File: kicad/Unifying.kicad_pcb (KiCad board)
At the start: 4 copper layers, 120.9 x 78.8 mm, 132 parts, among them J1 Conn_01x02, J10 GPDI0, J11 GPDI1, J12 nRpiBoot, J13 Conn_01x03, J14 Conn_01x03, J15 AudioOUT, J16 Micro_SD_Card_Det, J17 THD-20-R, J18 GLOBAL_EN, J19 AudioAMP, J2 Bus_M.2_Socket_B, J20 THD-02-R, J21 MIC, J3 USB_OTG, J4 Conn_01x04_Male, J5 USB_A, J6 USB_A, J7 USB_MICRO, J8 Conn_01x22_Female, J9 Conn_01x22_Female, Q1 DMP3013SFV-7, U1 TPD4EUSB30, U10 74LVC1G07SE-7, U11 RT9742GGJ5, U12 MagJack-A70-112-331N126, U2 AP64501SP-13, U3 FSUSB42MUX, U4 USB2514B-I/M2, U5 TPD4EUSB30, U6 AP22653W6, U7 RT9742SNGV, U8 74LVC1G07SE-7, U9 NC7WZ16, Y1 24MHz

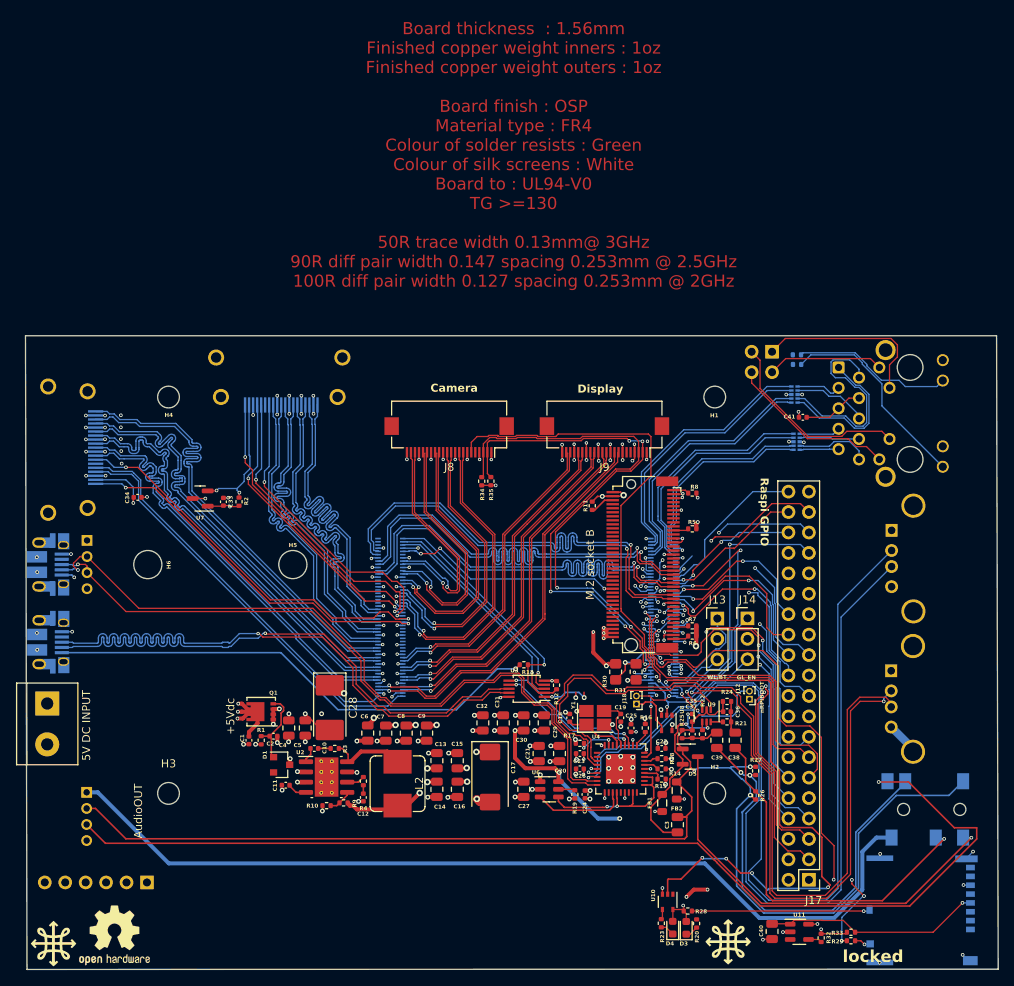
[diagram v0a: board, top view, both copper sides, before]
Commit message: Rounting all signals fix #16
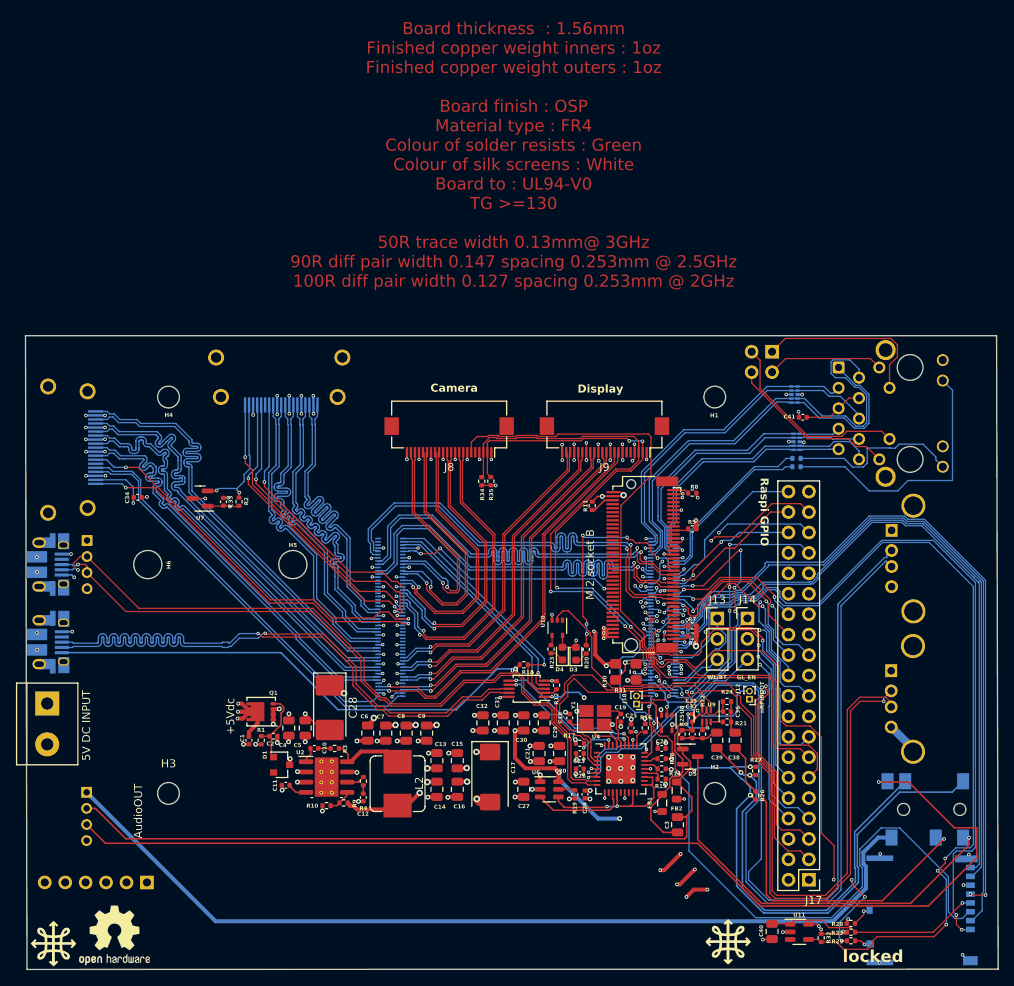
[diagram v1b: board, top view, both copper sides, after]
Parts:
- moved D3 36.7 mm to (165.2, 114.0)
- moved D4 36.7 mm to (163.5, 113.9)
- moved R20 36.7 mm to (166.5, 113.4)
- moved R23 36.7 mm to (162.1, 113.4)
- moved U10 36.7 mm to (162.9, 110.7)
- moved R28 20.3 mm to (199.4, 147.5)
- moved R36 13.9 mm to (192.6, 90.7)
- moved R37 11.7 mm to (192.7, 89.7)
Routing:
- net /CM4_GPIO (GPIO, SDCARD)/SD_PWR_ON: track 1.70 -> 114.2 mm, vias 0 -> 3
- net /CM4_GPIO (GPIO, SDCARD)/SD_DAT2: track 0.00 -> 95.3 mm, vias 0 -> 2
- net /CM4_GPIO (GPIO, SDCARD)/SD_DAT3: track 0.00 -> 91.8 mm
- net /CM4_GPIO (GPIO, SDCARD)/SD_CLK: track 0.00 -> 89.6 mm, vias 0 -> 2
- net /CM4_GPIO (GPIO, SDCARD)/SD_CMD: track 0.00 -> 88.2 mm, vias 0 -> 2
- net /CM4_GPIO (GPIO, SDCARD)/SD_DAT0: track 0.00 -> 85.8 mm
- net /CM4_GPIO (GPIO, SDCARD)/SD_DAT1: track 0.00 -> 85.3 mm
- net /CM4_GPIO (GPIO, SDCARD)/nPWR_LED: track 70.5 -> 22.5 mm, vias 5 -> 1
- net Net-(Module1A-PI_nLED_Activity): track 2.95 -> 28.3 mm, vias 0 -> 5
- net /CM4_GPIO (GPIO, SDCARD)/ETH_LEDY: track 0.00 -> 21.6 mm
- net /CM4_GPIO (GPIO, SDCARD)/ETH_LEDG: track 0.00 -> 21.4 mm
- net Net-(J16-DET_A): track 22.2 -> 2.80 mm
- net Net-(U12-LEDG_K): track 19.9 -> 33.6 mm
- net /USB2-HUB/VBUS: track 184.1 -> 190.5 mm, vias 8 -> 12
- net /CM4_GPIO (GPIO, SDCARD)/GPIO11: track 29.9 -> 26.1 mm
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
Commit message: Slightly improving routing
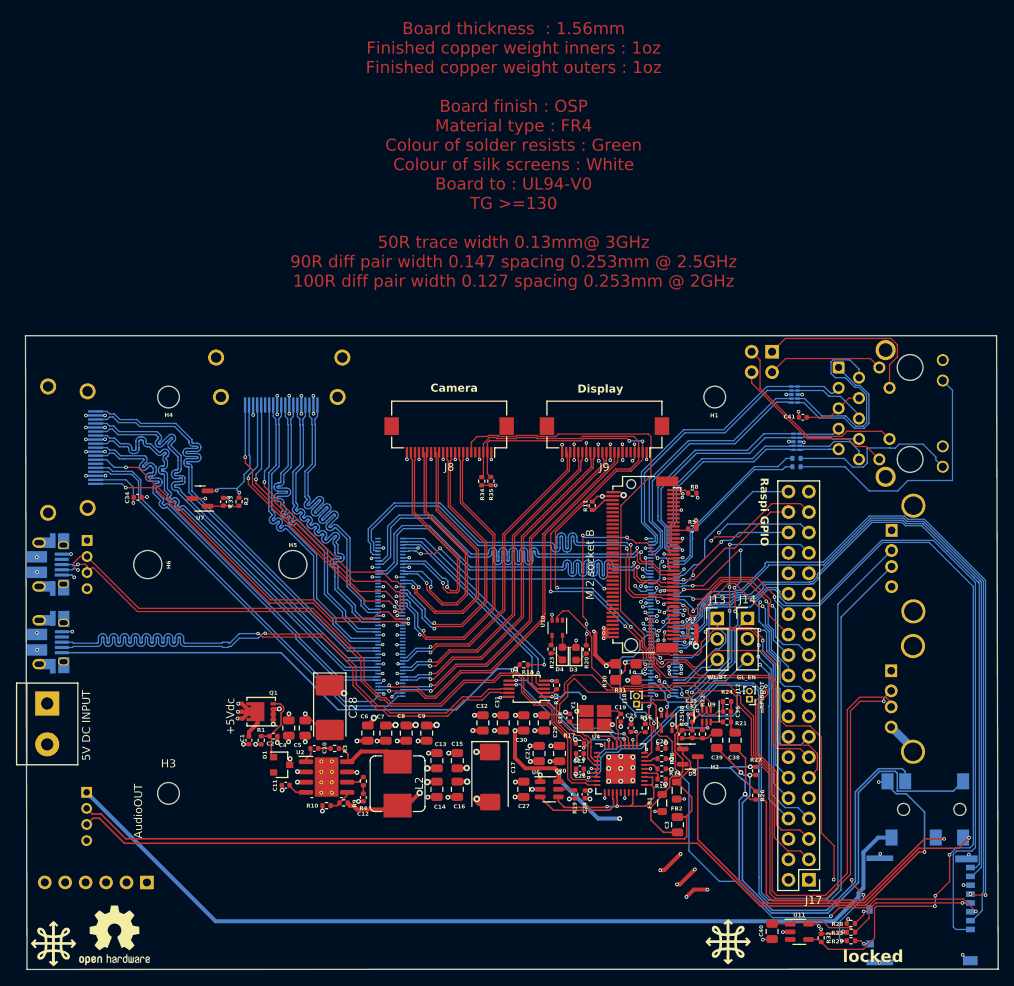
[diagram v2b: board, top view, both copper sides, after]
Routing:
- net Net-(J19-Pin_3): track 136.8 -> 124.4 mm, vias 1 -> 2
- net /CM4_GPIO (GPIO, SDCARD)/SD_CMD: track 88.2 -> 75.9 mm, vias 2 -> 4
- net Net-(D5-K)_1: track 169.2 -> 174.8 mm
- net /CM4_GPIO (GPIO, SDCARD)/AUDIO_R: track 53.1 -> 56.7 mm
- net /USB2-HUB/HD3_P: track 110.5 -> 107.7 mm
- net /USB2-HUB/HD3_N: track 110.6 -> 109.1 mm
- net /CM4_GPIO (GPIO, SDCARD)/SD_PWR_ON: track 114.2 -> 113.0 mm
- net /CM4_GPIO (GPIO, SDCARD)/SD_PWR: track 27.0 -> 27.7 mm
- net Net-(D5-K): track 52.0 -> 51.5 mm
- net /CM4_GPIO (GPIO, SDCARD)/SD_DAT2: track 95.3 -> 95.7 mm, vias 2 -> 0

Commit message: Adding/moving some text fix #19
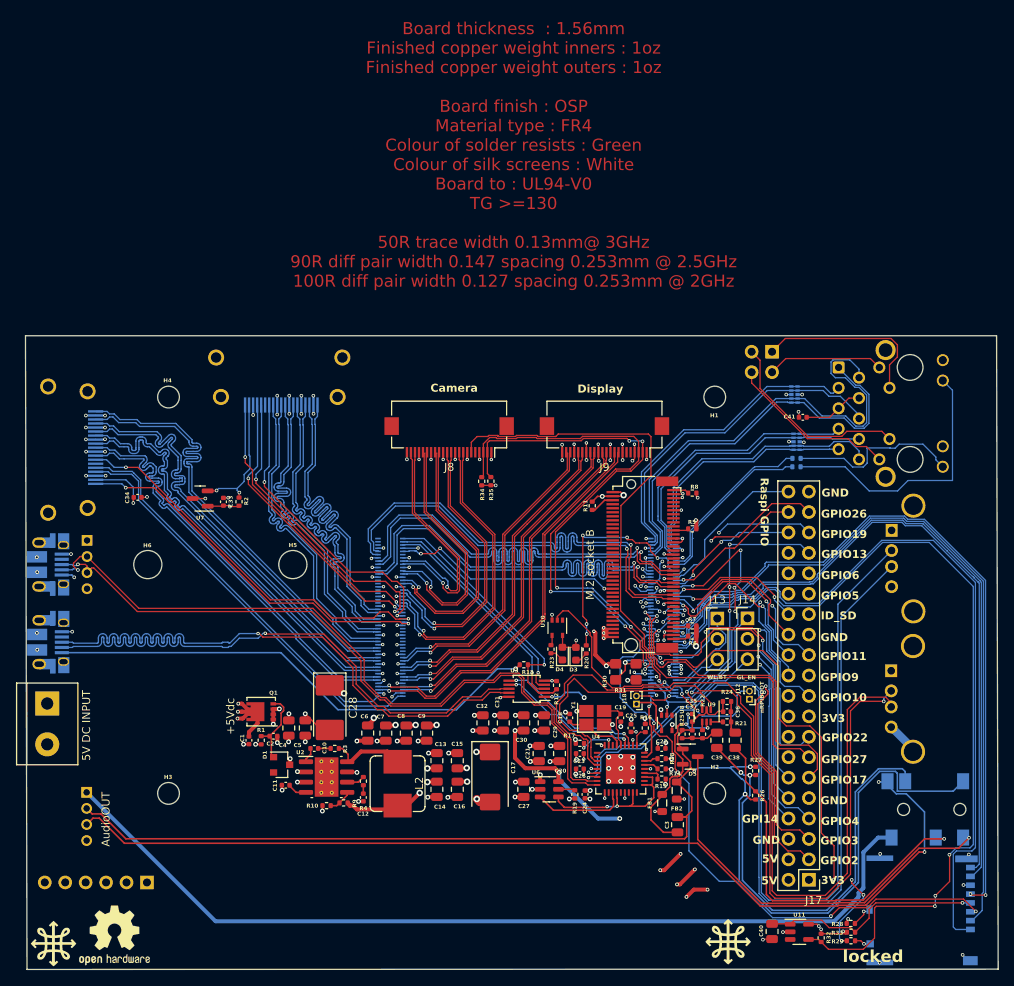
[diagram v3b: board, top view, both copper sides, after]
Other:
- board text added: "3V3"
- board text added: "5V"
- board text added: "GND"
- board text added: "GPI14"
- board text added: "GPIO10"
- board text added: "GPIO11"
- board text added: "GPIO13"
- board text added: "GPIO17"
- board text added: "GPIO19"
- board text added: "GPIO2"
- board text added: "GPIO22"
- board text added: "GPIO26"
- board text added: "GPIO27"
- board text added: "GPIO3"
- board text added: "GPIO4"
- board text added: "GPIO5"
- board text added: "GPIO6"
- board text added: "GPIO9"
- board text added: "ID_SD"
- board text added: "Microphone"
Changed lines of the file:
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@@
     (property "ki_description" "Mounting Hole without connection")
     (property "ki_keywords" "mounting hole")
-    (fp_text reference "H6" (at 2.601 0.04 90) (layer "F.SilkS")
+    (fp_text reference "H6" (at -0.059 -2.38 180) (layer "F.SilkS")
         (effects (font (size 0.5 0.5) (thickness 0.1) bold))
     )
@@
     (property "ki_description" "Mounting Hole without connection")
     (property "ki_keywords" "mounting hole")
-    (fp_text reference "H3" (at 0 -3.7) (layer "F.SilkS")
-        (effects (font (size 1 1) (thickness 0.15)))
+    (fp_text reference "H3" (at -0.052 -2.028) (layer "F.SilkS")
+        (effects (font (size 0.5 0.5) (thickness 0.1) bold))
     )
     (fp_text value "MountingHole" (at 0.068 0.762) (layer "F.Fab")
@@
     (property "ki_keywords" "cap capacitor")
     (attr smd)
-    (fp_text reference "C28" (at 0 -2.89 -90) (layer "F.SilkS")
+    (fp_text reference "C28" (at 0 -2.89 90) (layer "F.SilkS")
         (effects (font (size 1 1) (thickness 0.15)))
     )
-    (fp_text value "100uF" (at 0 2.7 -90) (layer "F.Fab")
+    (fp_text value "100uF" (at 0 2.7 90) (layer "F.Fab")
         (effects (font (size 1 1) (thickness 0.15)))
     )
-    (fp_text user "${REFERENCE}" (at 0 0 -90) (layer "F.Fab")
+    (fp_text user "${REFERENCE}" (at 0 0 90) (layer "F.Fab")
         (effects (font (size 1 1) (thickness 0.15)))
     )
@@
       (rotate (xyz 0 0 0))
     )
+    (model ":KICAD6_3DMODEL_DIR:Capacitor_Tantalum_SMD.3dshapes/CP_EIA-7343-20_Kemet-V.wrl"
+      (offset (xyz 0 0 0))
+      (scale (xyz 0.9 0.9 0.9))
+      (rotate (xyz 0 0 0))
+    )
   )
   (footprint "Capacitor_SMD:C_0402_1005Metric" (layer "F.Cu")
@@
     (property "ki_description" "Mounting Hole without connection")
     (property "ki_keywords" "mounting hole")
-    (fp_text reference "H4" (at 0.028 2.238) (layer "F.SilkS")
+    (fp_text reference "H4" (at -0.122 -2.062) (layer "F.SilkS")
         (effects (font (size 0.5 0.5) (thickness 0.1) bold))
     )
@@
         (effects (font (size 1 1) (thickness 0.15)) (justify mirror))
     )
-    (fp_text user "${VALUE}" (at -0.204 -97.843 90 unlocked) (layer "F.SilkS")
+    (fp_text user "${VALUE}" (at -1.22 -101.88 90 unlocked) (layer "F.SilkS")
         (effects (font (size 1 1) (thickness 0.15)))
     )
@@
     (property "Sheetname" "CM4_GPIO (GPIO, SDCARD)")
     (attr through_hole)
-    (fp_text reference "U12" (at 0.01 11.32 90) (layer "B.SilkS")
+    (fp_text reference "U12" (at -6.84 11.3925 90) (layer "B.SilkS")
         (effects (font (size 1 1) (thickness 0.15)) (justify mirror))
     )
@@
     (property "ki_keywords" "connector")
     (attr through_hole)
-    (fp_text reference "J21" (at 0 2.77 90) (layer "B.SilkS")
+    (fp_text reference "J21" (at -2.6 0.68 180) (layer "B.SilkS")
         (effects (font (size 1 1) (thickness 0.15)) (justify mirror))
     )
@@
     (effects (font (size 1 1) (thickness 0.15)) (justify mirror))
   )
-  (gr_text "GPDI1" (at 135.52 90.08) (layer "B.SilkS")
+  (gr_text "GPDI1" (at 135.46 85.29) (layer "B.SilkS")
     (effects (font (size 1 1) (thickness 0.2) bold) (justify mirror))
   )
-  (gr_text "USB3" (at 196.2 100.43 90) (layer "B.SilkS")
+  (gr_text "USB3" (at 212.5 94.51) (layer "B.SilkS")
     (effects (font (size 1 1) (thickness 0.2) bold) (justify mirror))
   )
+  (gr_text "Microphone" (at 113.62 140.42) (layer "B.SilkS")
+    (effects (font (size 1 1) (thickness 0.2) bold) (justify left bottom mirror))
+  )
   (gr_text "uSDCARD" (at 216.77 147.48 -90) (layer "B.SilkS")
     (effects (font (size 1 1) (thickness 0.2) bold) (justify mirror))
   )
-  (gr_text "GPDI0" (at 110.02 82.73 90) (layer "B.SilkS")
+  (gr_text "GPDI0" (at 107.83 81.66 90) (layer "B.SilkS")
     (effects (font (size 1 1) (thickness 0.2) bold) (justify mirror))
   )
-  (gr_text "USB2" (at 196.2 117.26 90) (layer "B.SilkS")
+  (gr_text "USB2" (at 212.62 112.27) (layer "B.SilkS")
     (effects (font (size 1 1) (thickness 0.2) bold) (justify mirror))
   )
@@
     (effects (font (size 2 2) (thickness 0.3)) (justify mirror))
   )
+  (gr_text "GPIO22" (at 195.81 124.96) (layer "F.SilkS")
+    (effects (font (size 1 1) (thickness 0.2) bold) (justify left bottom))
+  )
+  (gr_text "3V3" (at 195.68 142.69) (layer "F.SilkS")
+    (effects (font (size 1 1) (thickness 0.2) bold) (justify left bottom))
+  )
+  (gr_text "GPIO9" (at 195.63 117.46) (layer "F.SilkS")
+    (effects (font (size 1 1) (thickness 0.2) bold) (justify left bottom))
+  )
+  (gr_text "GPIO11" (at 195.64 114.85) (layer "F.SilkS")
+    (effects (font (size 1 1) (thickness 0.2) bold) (justify left bottom))
+  )
+  (gr_text "GND" (at 195.75 94.53) (layer "F.SilkS")
+    (effects (font (size 1 1) (thickness 0.2) bold) (justify left bottom))
+  )
+  (gr_text "GPIO5" (at 195.68 107.32) (layer "F.SilkS")
+    (effects (font (size 1 1) (thickness 0.2) bold) (justify left bottom))
+  )
+  (gr_text "3V3" (at 195.73 122.56) (layer "F.SilkS")
+    (effects (font (size 1 1) (thickness 0.2) bold) (justify left bottom))
+  )
+  (gr_text "GND" (at 195.64 112.5) (layer "F.SilkS")
+    (effects (font (size 1 1) (thickness 0.2) bold) (justify left bottom))
+  )
+  (gr_text "GPIO17" (at 195.71 130.22) (layer "F.SilkS")
+    (effects (font (size 1 1) (thickness 0.2) bold) (justify left bottom))
+  )
   (gr_text "Camera" (at 150.08 80.91) (layer "F.SilkS")
     (effects (font (size 1 1) (thickness 0.2) bold))
@@
     (effects (font (size 1 1) (thickness 0.2) bold))
   )
+  (gr_text "ID_SD" (at 195.65 109.8) (layer "F.SilkS")
+    (effects (font (size 1 1) (thickness 0.2) bold) (justify left bottom))
+  )
+  (gr_text "GPIO13" (at 195.72 102.16) (layer "F.SilkS")
+    (effects (font (size 1 1) (thickness 0.2) bold) (justify left bottom))
+  )
+  (gr_text "GPIO2" (at 195.61 140.24) (layer "F.SilkS")
+    (effects (font (size 1 1) (thickness 0.2) bold) (justify left bottom))
+  )
   (gr_text "nRPIBOOT" (at 188.36 119.35 90) (layer "F.SilkS")
     (effects (font (size 0.5 0.5) (thickness 0.1) bold))
@@
     (effects (font (size 1 1) (thickness 0.2) bold))
   )
+  (gr_text "GPIO19" (at 195.71 99.68) (layer "F.SilkS")
+    (effects (font (size 1 1) (thickness 0.2) bold) (justify left bottom))
+  )
   (gr_text locked "Unifying Balthazar Ver: 0.2" (at 202.16 151.57) (layer "F.SilkS")
     (effects (font (size 1.5 1.5) (thickness 0.3) bold))
@@
     (effects (font (size 1 1) (thickness 0.15)))
   )
+  (gr_text "GPIO27" (at 195.73 127.67) (layer "F.SilkS")
+    (effects (font (size 1 1) (thickness 0.2) bold) (justify left bottom))
+  )
+  (gr_text "GPIO4" (at 195.68 135.35) (layer "F.SilkS")
+    (effects (font (size 1 1) (thickness 0.2) bold) (justify left bottom))
+  )
+  (gr_text "GPIO6" (at 195.71 104.79) (layer "F.SilkS")
+    (effects (font (size 1 1) (thickness 0.2) bold) (justify left bottom))
+  )
+  (gr_text "GPI14" (at 185.85 135.07) (layer "F.SilkS")
+    (effects (font (size 1 1) (thickness 0.2) bold) (justify left bottom))
+  )
   (gr_text "5V DC INPUT" (at 104.36 122.86 90) (layer "F.SilkS")
     (effects (font (size 1 1) (thickness 0.15)))
   )
+  (gr_text "5V" (at 188.35 140.02) (layer "F.SilkS")
+    (effects (font (size 1 1) (thickness 0.2) bold) (justify left bottom))
+  )
+  (gr_text "GPIO10" (at 195.68 119.97) (layer "F.SilkS")
+    (effects (font (size 1 1) (thickness 0.2) bold) (justify left bottom))
+  )
+  (gr_text "GPIO3" (at 195.61 137.77) (layer "F.SilkS")
+    (effects (font (size 1 1) (thickness 0.2) bold) (justify left bottom))
+  )
+  (gr_text "GND" (at 195.63 132.78) (layer "F.SilkS")
+    (effects (font (size 1 1) (thickness 0.2) bold) (justify left bottom))
+  )
+  (gr_text "5V" (at 188.27 142.74) (layer "F.SilkS")
+    (effects (font (size 1 1) (thickness 0.2) bold) (justify left bottom))
+  )
   (gr_text "M.2 socket B" (at 166.99 102.86 90) (layer "F.SilkS")
     (effects (font (size 1 1) (thickness 0.15)))
   )
+  (gr_text "GND" (at 187.19 137.7) (layer "F.SilkS")
+    (effects (font (size 1 1) (thickness 0.2) bold) (justify left bottom))
+  )
+  (gr_text "GPIO26" (at 195.69 97.15) (layer "F.SilkS")
+    (effects (font (size 1 1) (thickness 0.2) bold) (justify left bottom))
+  )
   (dimension (type aligned) (layer "Dwgs.User")
